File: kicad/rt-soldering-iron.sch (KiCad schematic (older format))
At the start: 0 parts

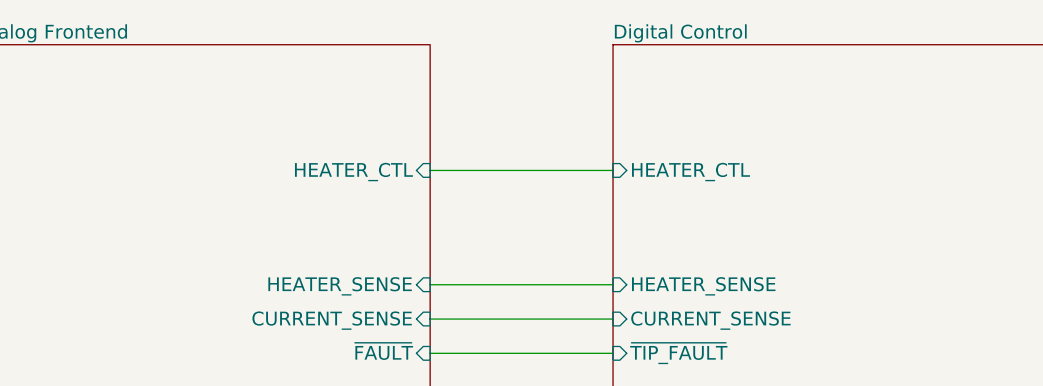
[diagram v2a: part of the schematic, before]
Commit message: Fixed thermal cutoff circuit and finished footprint selection
The main issue with the thermal cutoff was the open-collector maximum
voltage. I had to find a (slightly more expensive) comparator with an
output that was tolerant. Other comparators that would be instead
tolerant of being run off 12V were about the same price.

The fuse I'm not sure about. I'm just going to short it out. The
regulator can handle a short circuit and so can the crowbar. I also
couldn't decide where to put the feedback network. If I put it after the
fuse it would compensate for any voltage drop across it. However, it
would also cause the regulator to try to boost the voltage insanely high
during a short circuit across the fuse and maybe cause it to pop (I
could really only find ones rated to 6V). I instead placed it before the
fuse. I'm still not sure.
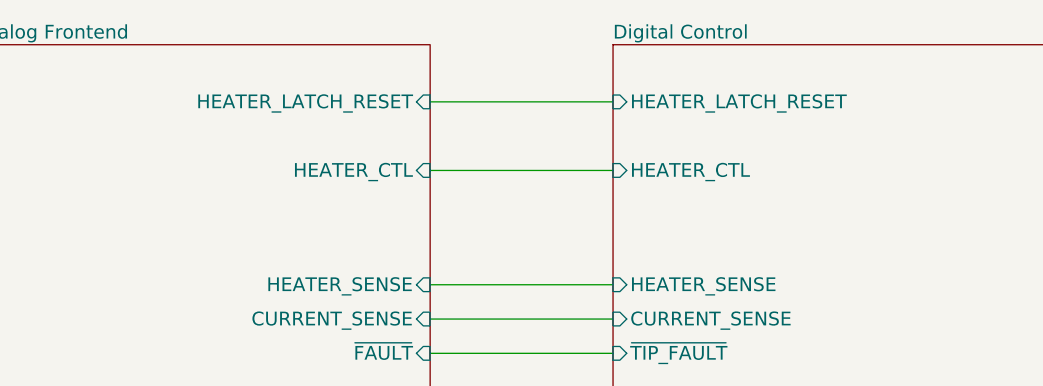
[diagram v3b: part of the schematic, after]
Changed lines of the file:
@@
 F4 "CURRENT_SENSE" I R 4600 3000 60
 F5 "~FAULT" I R 4600 3150 60
+F6 "HEATER_LATCH_RESET" I R 4600 2050 60
 $EndSheet
 $Sheet
@@
 F4 "CURRENT_SENSE" I L 5400 3000 60
 F5 "~TIP_FAULT" I L 5400 3150 60
+F6 "HEATER_LATCH_RESET" I L 5400 2050 60
 $EndSheet
 Wire Wire Line
@@
 Wire Wire Line
 	5400 3150 4600 3150
+Wire Wire Line
+	5400 2050 4600 2050
 $EndSCHEMATC
